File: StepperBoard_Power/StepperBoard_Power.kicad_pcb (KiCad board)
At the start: 2 copper layers, 56 x 56 mm, 65 parts, among them IC1 A4989SLDTR-T, J1 Conn_02x05_Odd_Even, J2 Conn_02x05_Odd_Even, J3 Conn_02x06, J4 Screw_Terminal_01x04, Q1 DMNH10H028SK3Q-13, Q2 DMNH10H028SK3Q-13, Q3 DMNH10H028SK3Q-13, Q4 DMNH10H028SK3Q-13, Q5 DMNH10H028SK3Q-13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

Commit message: Updated version on GitHub
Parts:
- removed C7: 100u, Capacitor_SMD:C_0402_1005Metric
- removed C8: 10n, Capacitor_SMD:C_0402_1005Metric
- added C17: 100u, Capacitor_SMD:C_0402_1005Metric, F.Cu at (147.0, 105.0)
- added C18: 100u, Capacitor_SMD:C_0402_1005Metric, F.Cu at (135.5, 101.5)
- added D1: LED, LED_SMD:LED_0201_0603Metric, F.Cu at (124.0, 94.0)
- added F1: Fuse, Fuse:Fuse_BelFuse_0ZRE0012FF_L8.3mm_W3.8mm, F.Cu at (133.0, 97.0)
- added IC2: VN7007ALHTR, CustomFootprint:OCTAPAK, F.Cu at (137.0, 88.8)
- added IC3: MCS1802GS-20-Z, CustomFootprint:SOIC127P600X175-8N, F.Cu at (148.5, 78.5)
- added R_SENSE1: 0.05, Resistor_SMD:R_0612_1632Metric, F.Cu at (155.8, 97.5)
- added R_SENSE2: 0.05, Resistor_SMD:R_0612_1632Metric, F.Cu at (155.8, 102.0)
- C1, C3: value 100u -> 68u @ 50V; footprint Capacitor_SMD:C_0402_1005Metric -> Capacitor_SMD:CP_Elec_6.3x7.7
- C12: value 100u -> 10u; footprint Capacitor_SMD:C_0402_1005Metric -> Capacitor_SMD:C_0805_2012Metric
- C13: value 10u -> 100u; footprint Capacitor_SMD:C_0805_2012Metric -> Capacitor_SMD:C_0402_1005Metric
- C14, C15: value 100u -> C
- C4: value 1000u @ 50V -> 10n; footprint Capacitor_THT:CP_Radial_D12.5mm_P5.00mm -> Capacitor_SMD:C_0402_1005Metric
- J1: value Conn_02x05_Odd_Even -> Screw_Terminal_01x02; footprint Connector_PinHeader_1.27mm:PinHeader_2x05_P1.27mm_Vertical_SMD -> TerminalBlock_Phoenix:TerminalBlock_Phoenix_PT-1,5-2-3.5-H_1x02_P3.50mm_Horizontal; moved to F.Cu
- J2: moved to F.Cu
- J3: value Conn_02x06 -> Conn_02x05_Odd_Even; footprint Connector_PinHeader_1.27mm:PinHeader_2x06_P1.27mm_Vertical_SMD -> Connector_PinHeader_1.27mm:PinHeader_2x05_P1.27mm_Vertical_SMD; moved to F.Cu
- JP1, JP2, JP3, JP4: value SolderJumper_2_Open -> SolderJumper_3_Bridged12; footprint Jumper:SolderJumper-2_P1.3mm_Open_RoundedPad1.0x1.5mm -> Jumper:SolderJumper-3_P1.3mm_Bridged2Bar12_RoundedPad1.0x1.5mm_NumberLabels
- Q1, Q2, Q3, Q4, Q5, Q6, Q7, Q8: footprint Package_TO_SOT_SMD:TO-252-3_TabPin2 -> CustomFootprint:TO-252-2 Tab1
- R22: value 0.03 -> 15k
- R23: value 22k -> 10k
- R24: value 2k2 -> 22k
- R25: value 10k -> 3k3
- R7: value 500k -> 3.3k
- R9: value 0.03 -> 500k
- RV1: value 20k -> 30k
- SW1, SW2: footprint Button_Switch_SMD:SW_DIP_SPSTx02_Slide_6.7x6.64mm_W8.61mm_P2.54mm_LowProfile -> Button_Switch_SMD:SW_DIP_SPSTx02_Slide_Copal_CHS-02A_W5.08mm_P1.27mm_JPin
- moved H3 153.0 mm to (174.5, 124.5)
- moved H2 142.2 mm to (174.5, 75.5)
- moved H4 105.4 mm to (125.5, 124.5)
- moved H1 95.7 mm to (125.5, 75.5)
- moved R1 79.1 mm to (176.0, 92.0), turned to 180 degrees
- moved R16 78.1 mm to (176.5, 109.0), turned to 0 degrees
- moved R10 75.5 mm to (176.5, 108.0), turned to 180 degrees
- moved R3 75.3 mm to (176.0, 91.0), turned to 180 degrees
- moved R17 70.1 mm to (169.0, 115.0), turned to 180 degrees
- moved R11 68.7 mm to (169.5, 118.0)
- moved R4 67.6 mm to (169.0, 85.0), turned to 0 degrees
- moved R2 63.7 mm to (160.5, 83.5), turned to 0 degrees
- moved R9 57.7 mm to (157.0, 93.5), turned to -90 degrees
- moved R8 55.5 mm to (152.0, 88.0)
- moved R15 53.0 mm to (144.0, 121.5)
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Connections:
- C1 pad 1: +24V -> VDDF
- C12 pad 1: VRef -> Net-(IC1-VREG)
- C13 pad 1: Net-(IC1-VREG) -> GND
- C13 pad 2: GND -> +24V
- C14 pad 1: GND -> +3.3V
- C14 pad 2: +24V -> GND
- C15 pad 1: Bridge1_CA -> Net-(IC3-FILT)
- C15 pad 2: Net-(IC1-C1A) -> GND
- C16 pad 1: Bridge1_CB -> Bridge1_CA
- C16 pad 2: Net-(IC1-C1B) -> Net-(IC1-C1A)
- C3 pad 1: +24V -> VDDF
- J1 pad 1: +3.3V -> VCC
- J1 pad 2: +24V -> GND
- J2 pad 2: +24V -> +3.3V
- J2 pad 3: PFD1 -> DIR
- J2 pad 4: MS2 -> STP
- J2 pad 5: PFD2 -> EN
- J2 pad 6: MS1 -> RST
- J2 pad 7: GND -> Switch_uC
- J2 pad 8: GND -> Sense_uC
- J3 pad 1: +24V -> +3.3V
- J3 pad 2: +24V -> +3.3V
- J3 pad 3: +24V -> PFD1_uC
- J3 pad 4: +24V -> MS2_uC
- J3 pad 5: +24V -> PFD2_uC
- J3 pad 6: +24V -> MS1_uC
- J4 pad 1: W2_1 -> Bridge2_CB
- J4 pad 2: W2_2 -> Bridge2_CA
- J4 pad 3: W1_1 -> Bridge1_CB
- J4 pad 4: W1_2 -> Bridge1_CA
- JP1 pad 1: MS1 -> Net-(JP1-A)
- JP1 pad 2: Net-(JP1-B) -> MS1
- JP3 pad 1: PFD1 -> Net-(JP3-A)
- JP3 pad 2: Net-(JP3-B) -> PFD1
- Q1 pad 1: +24V -> VDDF
- Q2 pad 1: +24V -> VDDF
- Q5 pad 1: +24V -> VDDF
- Q6 pad 1: +24V -> VDDF
- R12 pad 2: Net-(JP1-B) -> Net-(JP1-A)
- R13 pad 2: Net-(JP2-A) -> Net-(JP3-A)
- R14 pad 2: Net-(JP3-B) -> Net-(JP2-A)
- R22 pad 1: GND -> Switch_uC
- R22 pad 2: LSS2 -> Net-(IC2-INPUT)
- R23 pad 1: VRef -> Net-(IC1-OSC)
- R23 pad 2: +3.3V -> GND
- R24 pad 1: GND -> VRef
- R24 pad 2: Net-(R24-Pad2) -> +3.3V
- R25 pad 1: Net-(IC1-OSC) -> GND
- R25 pad 2: GND -> Net-(R25-Pad2)
- R7 pad 1: LSS1 -> Net-(D1-K)
- R7 pad 2: Net-(Q3-G) -> GND
- R8 pad 1: Net-(Q4-G) -> LSS1
- R8 pad 2: LSS1 -> Net-(Q3-G)
- R9 pad 1: GND -> Net-(Q4-G)
- RV1 pad 2: Net-(R24-Pad2) -> Net-(R25-Pad2)
- RV1 pad 3: Net-(R24-Pad2) -> Net-(R25-Pad2)
- SW1 pad 4: Net-(JP1-B) -> Net-(JP1-A)
- SW2 pad 4: Net-(JP3-B) -> Net-(JP3-A)

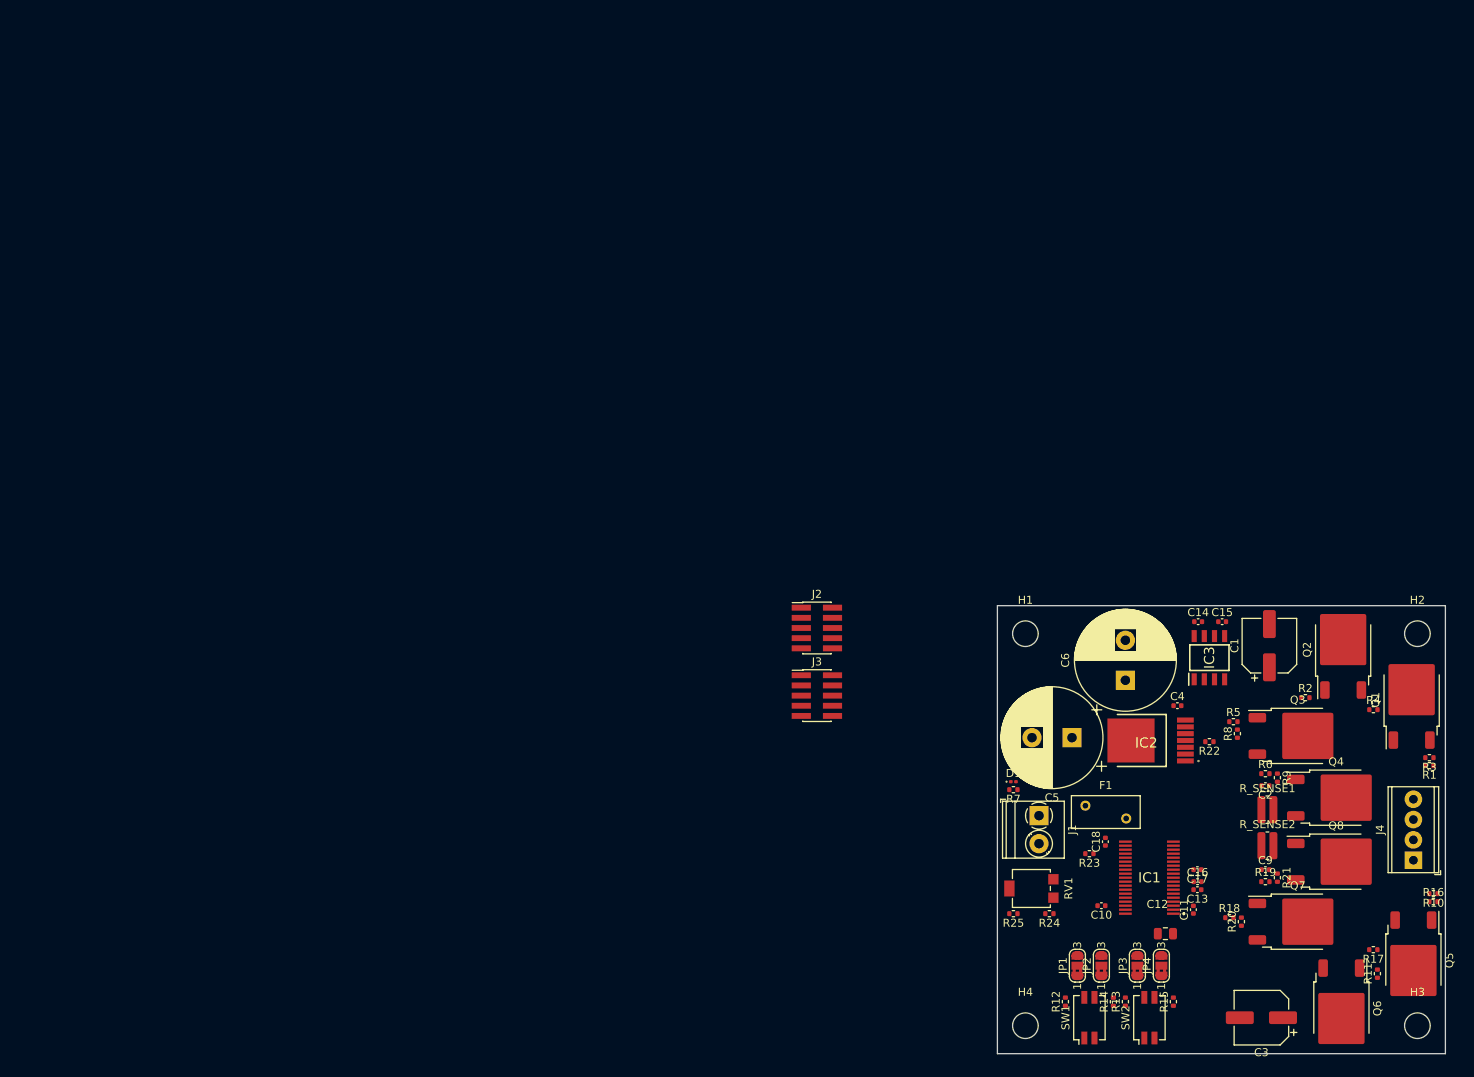
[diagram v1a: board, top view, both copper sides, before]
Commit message: Added NetTies and NetClasses
Added the NetTies library in CommonComponents folder and defined some NetClasses.
Also fixed the position of some components.
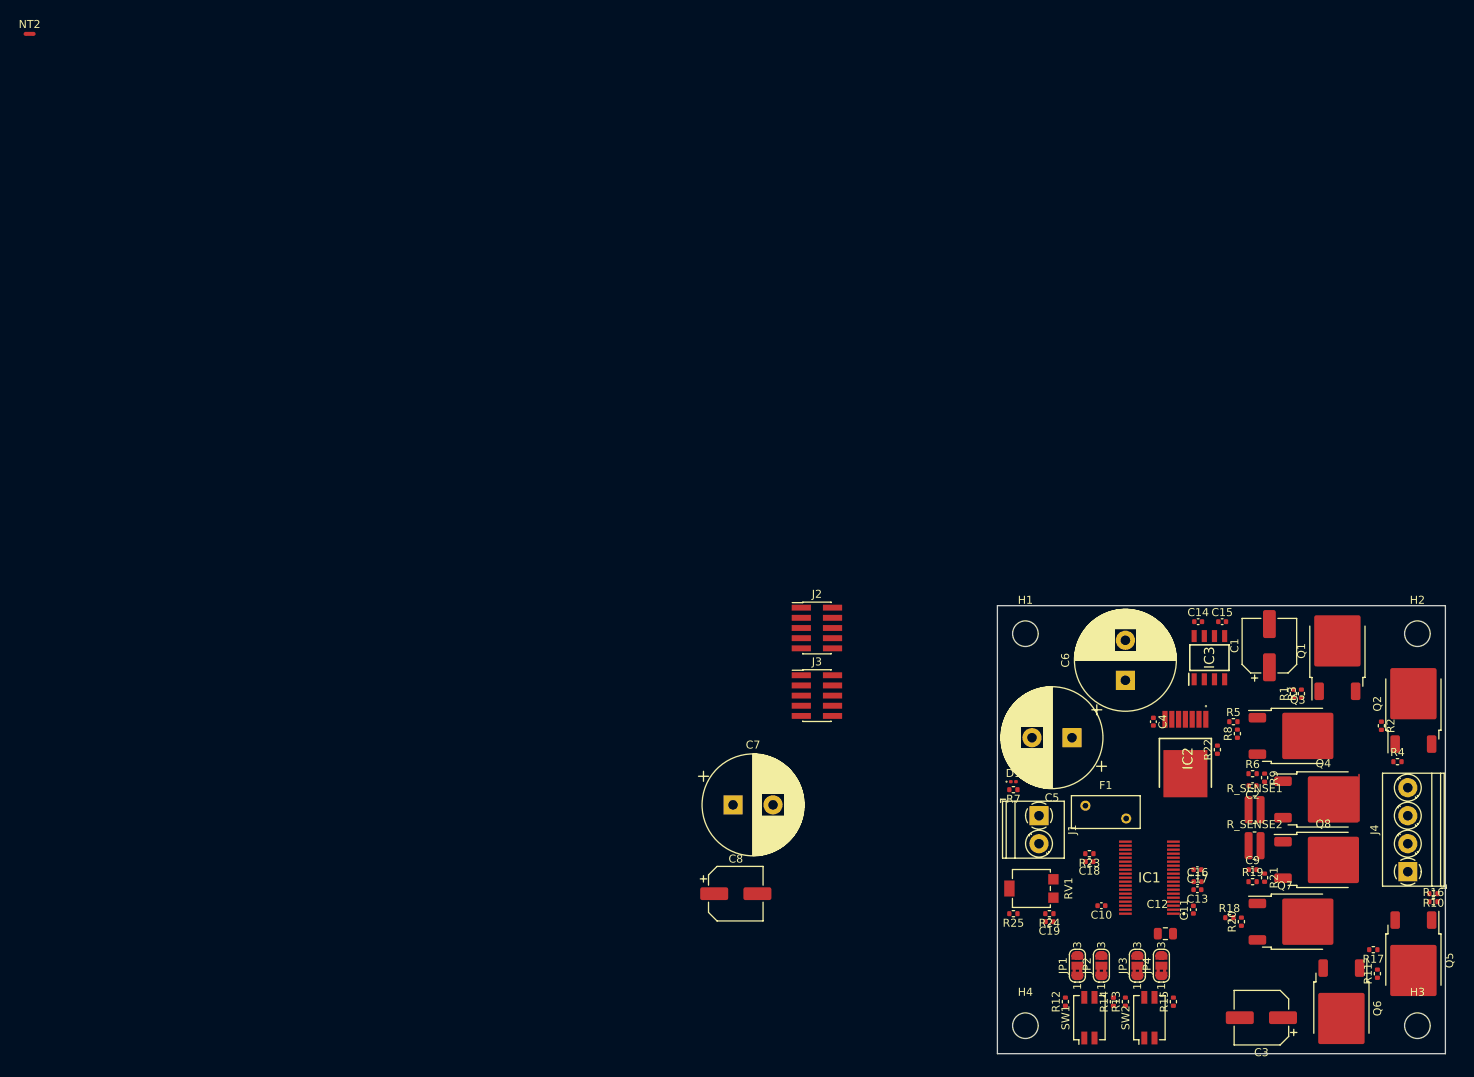
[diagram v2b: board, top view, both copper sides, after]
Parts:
- added C19: 100u, Capacitor_SMD:C_0402_1005Metric, F.Cu at (128.5, 111.5)
- added C7: 1000u @ 50V, Capacitor_THT:CP_Radial_D12.5mm_P5.00mm, F.Cu at (89.0, 96.9)
- added C8: 68u @ 50V, Capacitor_SMD:CP_Elec_6.3x7.7, F.Cu at (89.3, 108.0)
- added NT1: NetTie_2, NetTies:NetTie-2_SMD_Pad0.2mm, F.Cu at (125.8, 94.0)
- added NT2: NetTie_2, NetTies:NetTie-2_SMD_Pad0.5mm, F.Cu at (1.02, 0.53)
- C13: value 100u -> 100n
- C18: value 100u -> 10n
- J4: footprint TerminalBlock_Phoenix:TerminalBlock_Phoenix_MPT-0,5-4-2.54_1x04_P2.54mm_Horizontal -> TerminalBlock_Phoenix:TerminalBlock_Phoenix_PT-1,5-4-3.5-H_1x04_P3.50mm_Horizontal
- moved R1 19.2 mm to (159.0, 83.0), turned to 90 degrees
- moved R3 17.9 mm to (160.0, 83.0), turned to 90 degrees
- moved Q1 11.1 mm to (164.5, 77.7)
- moved Q2 11.1 mm to (174.0, 84.3)
- moved IC2 10.3 mm to (145.5, 94.7), turned to -90 degrees
- moved R2 10.1 mm to (170.0, 87.0), turned to -90 degrees
- moved R4 7.16 mm to (172.0, 91.5)
- moved C4 3.61 mm to (141.5, 86.5), turned to -90 degrees
- moved C18 3.20 mm to (133.5, 104.0), turned to 180 degrees
- moved Q4 1.62 mm to (162.7, 96.2)
- moved Q8 1.62 mm to (162.7, 103.8)
- moved C2 1.60 mm to (153.9, 94.5)
- moved C9 1.60 mm to (153.9, 105.0)
- moved R19 1.60 mm to (153.9, 106.5)
- moved R21 1.60 mm to (155.4, 106.0)
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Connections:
- C12 pad 2: GND -> GNDD
- C13 pad 1: GND -> GNDD
- C14 pad 2: GND -> GNDD
- C15 pad 2: GND -> GNDD
- C18 pad 1: VRef -> +3.3V
- C18 pad 2: GND -> GNDD
- D1 pad 2: +24V -> Net-(D1-A)
- IC1 pad 20: GND -> GNDD
- IC2 pad 7: GND -> GNDD
- IC3 pad 5: GND -> GNDD
- J2 pad 10: GND -> GNDD
- J2 pad 9: GND -> GNDD
- J3 pad 10: GND -> GNDD
- J3 pad 7: GND -> GNDD
- J3 pad 8: GND -> GNDD
- J3 pad 9: GND -> GNDD
- R23 pad 2: GND -> GNDD
- R25 pad 1: GND -> GNDD
- R7 pad 2: GND -> GNDD
- SW1 pad 1: GND -> GNDD
- SW1 pad 2: GND -> GNDD
- SW2 pad 1: GND -> GNDD
- SW2 pad 2: GND -> GNDD
